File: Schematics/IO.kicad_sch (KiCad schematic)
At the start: 11 parts, among them J3 USB_B_Micro, J4 AVR-ISP-6, SW1 Rest, SW2 PEN, SW3 Fan, SW4 Servo

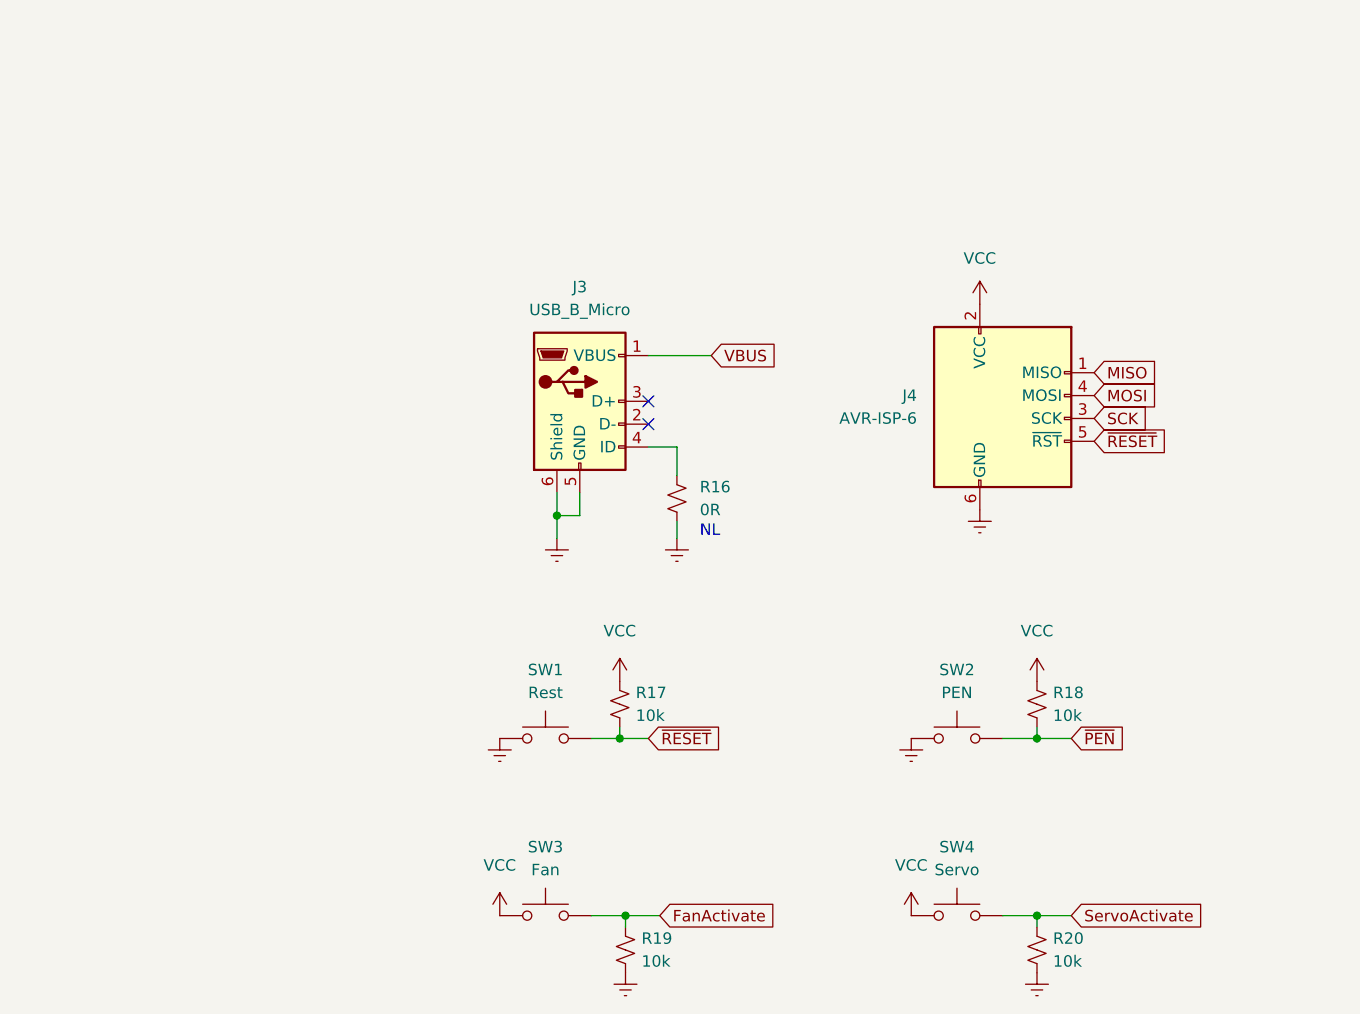
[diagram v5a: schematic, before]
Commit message: Fixed IR Sensor
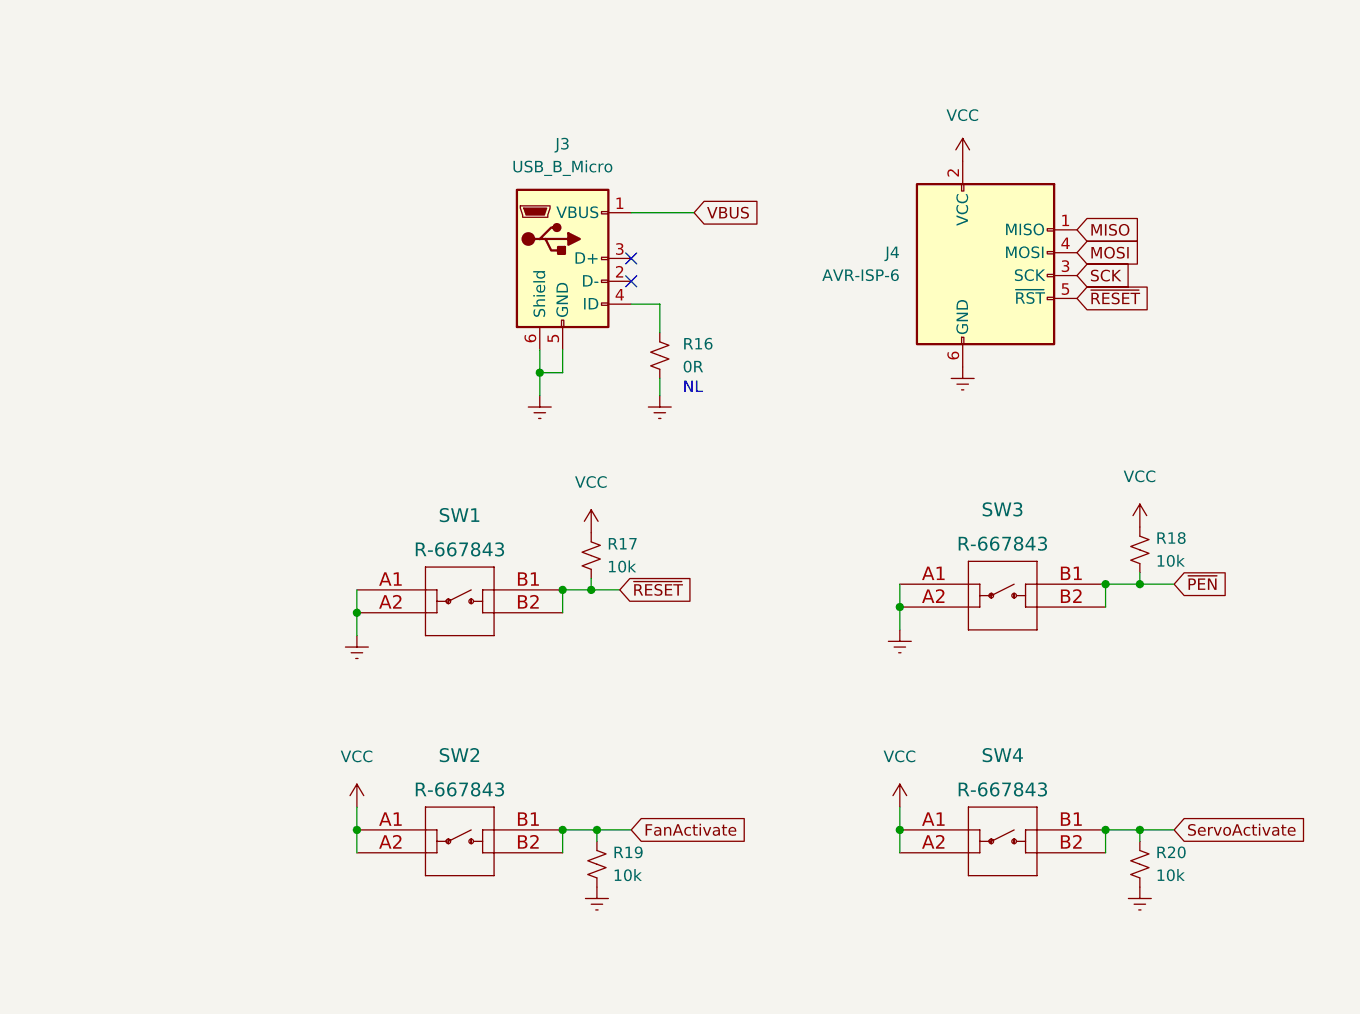
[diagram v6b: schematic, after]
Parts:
- removed SW1: Rest, SFRFootprints:R-667843, symbol Switch:SW_MEC_5G
- removed SW2: PEN, SFRFootprints:R-667843, symbol Switch:SW_MEC_5G
- removed SW3: Fan, SFRFootprints:R-667843, symbol Switch:SW_MEC_5G
- removed SW4: Servo, SFRFootprints:R-667843, symbol Switch:SW_MEC_5G
- added SW1, SW2, SW3, SW4: R-667843, SFRFootprints:R-667843, symbol SFRLibraries:R-667843
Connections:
- net Earth: now also SW1.A1, SW1.A2, SW3.A1, SW3.A2
- net FanActivate: now also SW2.B1, SW2.B2
- net ServoActivate: now also SW4.B1, SW4.B2
- net VCC: now also SW2.A1, SW2.A2, SW4.A1, SW4.A2
- net ~{PEN}: now also SW3.B1, SW3.B2
- net ~{RESET}: now also SW1.B1, SW1.B2
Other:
- moved on the sheet: J3, J4, R16, R17, R18, R19, R20
